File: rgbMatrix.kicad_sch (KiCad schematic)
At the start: 166 parts

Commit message: Right LED Driver almost connected
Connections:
- net CS1: now also R_B1.1; no longer R_G1.1
- net CS10: now also R_B4.1; no longer R_G4.1
- net CS12: now also R_G4.1; no longer R_B4.1
- net CS13: now also R_B5.1; no longer R_G5.1
- net CS15: now also R_G5.1; no longer R_B5.1
- net CS16: now also R_B6.1; no longer R_G6.1
- net CS18: now also R_G6.1; no longer R_B6.1
- net CS19: now also R_B7.1; no longer R_G7.1
- net CS21: now also R_G7.1; no longer R_B7.1
- net CS22: now also R_B8.1; no longer R_G8.1
- net CS24: now also R_G8.1; no longer R_B8.1
- net CS25: now also R_B9.1; no longer R_G9.1
- net CS27: now also R_G9.1; no longer R_B9.1
- net CS28: now also R_B10.1; no longer R_G10.1
- net CS3: now also R_G1.1; no longer R_B1.1
- net CS30: now also R_G10.1; no longer R_B10.1
- net CS4: now also R_B2.1; no longer R_G2.1
- net CS40: now also R_B11.1; no longer R_G17.1
- net CS41: now also R_R11.1; no longer R_R17.1
- net CS42: now also R_G11.1; no longer R_B17.1
- net CS43: now also R_B12.1; no longer R_G16.1
- net CS44: now also R_R12.1; no longer R_R16.1
- net CS45: now also R_G12.1; no longer R_B16.1
- net CS46: now also R_B13.1; no longer R_G15.1
- net CS47: now also R_R13.1; no longer R_R15.1
- net CS48: now also R_G13.1; no longer R_B15.1
- net CS49: now also R_B14.1; no longer R_G14.1
- net CS51: now also R_G14.1; no longer R_B14.1
- net CS52: now also R_B15.1; no longer R_G13.1
- net CS53: now also R_R15.1; no longer R_R13.1
- net CS54: now also R_G15.1; no longer R_B13.1
- net CS55: now also R_B16.1; no longer R_G12.1
- net CS56: now also R_R16.1; no longer R_R12.1
- net CS57: now also R_G16.1; no longer R_B12.1
- net CS58: now also R_B17.1; no longer R_G11.1
- net CS59: now also R_R17.1; no longer R_R11.1
- net CS6: now also R_G2.1; no longer R_B2.1
- net CS60: now also R_G17.1; no longer R_B11.1
- net CS7: now also R_B3.1; no longer R_G3.1
- net CS9: now also R_G3.1; no longer R_B3.1

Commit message: Routing Finished
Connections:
- net CS1: now also R_B9.1; no longer R_B1.1
- net CS10: now also R_B2.1; no longer R_B4.1
- net CS11: now also R_R2.1; no longer R_R4.1
- net CS12: now also R_G2.1; no longer R_G4.1
- net CS13: now also R_B3.1; no longer R_B5.1
- net CS14: now also R_R3.1; no longer R_R5.1
- net CS15: now also R_G3.1; no longer R_G5.1
- net CS16: now also R_B4.1; no longer R_B6.1
- net CS17: now also R_R4.1; no longer R_R6.1
- net CS18: now also R_G4.1; no longer R_G6.1
- net CS19: now also R_B5.1; no longer R_B7.1
- net CS2: now also R_R9.1; no longer R_R1.1
- net CS20: now also R_R5.1; no longer R_R7.1
- net CS21: now also R_G5.1; no longer R_G7.1
- net CS22: now also R_B6.1; no longer R_B8.1
- net CS23: now also R_R6.1; no longer R_R8.1
- net CS24: now also R_G6.1; no longer R_G8.1
- net CS25: now also R_B7.1; no longer R_B9.1
- net CS26: now also R_R7.1; no longer R_R9.1
- net CS27: now also R_G7.1; no longer R_G9.1
- net CS28: now also R_B8.1; no longer R_B10.1
- net CS29: now also R_R8.1; no longer R_R10.1
- net CS3: now also R_G9.1; no longer R_G1.1
- net CS30: now also R_G8.1; no longer R_G10.1
- net CS4: now also R_B10.1; no longer R_B2.1
- net CS5: now also R_R10.1; no longer R_R2.1
- net CS6: now also R_G10.1; no longer R_G2.1
- net CS7: now also R_B1.1; no longer R_B3.1
- net CS8: now also R_R1.1; no longer R_R3.1
- net CS9: now also R_G1.1; no longer R_G3.1

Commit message: Rearranged LED Drivers
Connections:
- net CS1: now also R_B7.1; no longer R_B9.1
- net CS10: now also R_B10.1; no longer R_B2.1
- net CS11: now also R_R10.1; no longer R_R2.1
- net CS12: now also R_G10.1; no longer R_G2.1
- net CS13: now also R_B1.1; no longer R_B3.1
- net CS14: now also R_R1.1; no longer R_R3.1
- net CS15: now also R_G1.1; no longer R_G3.1
- net CS16: now also R_B2.1; no longer R_B4.1
- net CS17: now also R_R2.1; no longer R_R4.1
- net CS18: now also R_G2.1; no longer R_G4.1
- net CS19: now also R_B3.1; no longer R_B5.1
- net CS2: now also R_R7.1; no longer R_R9.1
- net CS20: now also R_R3.1; no longer R_R5.1
- net CS21: now also R_G3.1; no longer R_G5.1
- net CS22: now also R_B4.1; no longer R_B6.1
- net CS23: now also R_R4.1; no longer R_R6.1
- net CS24: now also R_G4.1; no longer R_G6.1
- net CS25: now also R_B5.1; no longer R_B7.1
- net CS26: now also R_R5.1; no longer R_R7.1
- net CS27: now also R_G5.1; no longer R_G7.1
- net CS28: now also R_B6.1; no longer R_B8.1
- net CS29: now also R_R6.1; no longer R_R8.1
- net CS3: now also R_G7.1; no longer R_G9.1
- net CS30: now also R_G6.1; no longer R_G8.1
- net CS31: now also R_B15.1; no longer R_B18.1
- net CS32: now also R_G15.1; no longer R_R18.1
- net CS33: now also R_R15.1; no longer R_G18.1
- net CS34: now also R_B16.1; no longer R_B19.1
- net CS35: now also R_G16.1; no longer R_R19.1
- net CS36: now also R_R16.1; no longer R_G19.1
- net CS37: now also R_B17.1; no longer R_R20.1
- net CS38: now also R_G17.1; no longer R_G20.1
- net CS39: now also R_R17.1; no longer R_B20.1
- net CS4: now also R_B8.1; no longer R_B10.1
- net CS40: now also R_B18.1; no longer R_B11.1
- net CS41: now also R_R18.1; no longer R_R11.1
- net CS42: now also R_G18.1; no longer R_G11.1
- net CS43: now also R_B19.1; no longer R_B12.1
- net CS44: now also R_R19.1; no longer R_R12.1
- net CS45: now also R_G19.1; no longer R_G12.1
- net CS46: now also R_R20.1; no longer R_B13.1
- net CS47: now also R_G20.1; no longer R_R13.1
- net CS48: now also R_B20.1; no longer R_G13.1
- net CS49: now also R_B11.1; no longer R_B14.1
- net CS5: now also R_R8.1; no longer R_R10.1
- net CS50: now also R_R11.1; no longer R_R14.1
- net CS51: now also R_G11.1; no longer R_G14.1
- net CS52: now also R_B12.1; no longer R_B15.1
- net CS53: now also R_R12.1; no longer R_R15.1
- net CS54: now also R_G12.1; no longer R_G15.1
- net CS55: now also R_B13.1; no longer R_B16.1
- net CS56: now also R_R13.1; no longer R_R16.1
- net CS57: now also R_G13.1; no longer R_G16.1
- net CS58: now also R_B14.1; no longer R_B17.1
- net CS59: now also R_R14.1; no longer R_R17.1
- net CS6: now also R_G8.1; no longer R_G10.1
- net CS60: now also R_G14.1; no longer R_G17.1
- net CS7: now also R_B9.1; no longer R_B1.1
- net CS8: now also R_R9.1; no longer R_R1.1
- net CS9: now also R_G9.1; no longer R_G1.1

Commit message: Added RGB Underglow
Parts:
- added C18, C32, C34, C35, C36, C37, C38, C39, C40, C41, C42, C43, C44, C45: 104, Capacitor_SMD:C_0805_2012Metric_Pad1.18x1.45mm_HandSolder, symbol Device:C_Small
- added LED107, LED108, LED109, LED110, LED111, LED112, LED113, LED114, LED115, LED116, LED117, LED118, LED119, LED120: IN-PI55TATPRPGPB, ul_IN-PI55TATPRPGPB:IN-PI55TATPRPGPB, symbol ul_IN-PI55TATPRPGPB:IN-PI55TATPRPGPB
- added R3, R4: 500, Resistor_SMD:R_0805_2012Metric_Pad1.20x1.40mm_HandSolder, symbol Device:R_Small
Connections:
- new net: LED109.4 (DIN), LED117.2 (DOUT)
- new net: LED117.4 (DIN), LED118.2 (DOUT)
- new net: LED113.4 (DIN), LED120.2 (DOUT)
- new net: LED119.2 (DOUT), LED120.4 (DIN)
- new net: LED107.2 (DOUT), LED110.4 (DIN)
- new net: LED107.4 (DIN), LED108.2 (DOUT)
- new net: LED112.4 (DIN), LED113.2 (DOUT)
- new net: LED115.2 (DOUT), LED116.4 (DIN)
- new net: LED114.2 (DOUT), LED115.4 (DIN)
- new net: LED116.2 (DOUT), LED119.4 (DIN)
- new net: LED108.4 (DIN), LED109.2 (DOUT)
- new net: LED118.4 (DIN), R3.2
- new net: LED111.2 (DOUT), LED114.4 (DIN)
- new net: LED112.2 (DOUT), R4.2
- new net: LED110.2 (DOUT), LED111.4 (DIN)
- new net +5V: C18.1, C32.1, C34.1, C35.1, C36.1, C37.1, C38.1, C39.1, C40.1, C41.1, C42.1, C43.1, C44.1, C45.1, LED107.1 (VDD), LED108.1 (VDD), LED109.1 (VDD), LED110.1 (VDD), LED111.1 (VDD), LED112.1 (VDD), LED113.1 (VDD), LED114.1 (VDD), LED115.1 (VDD), LED116.1 (VDD), LED117.1 (VDD), LED118.1 (VDD), LED119.1 (VDD), LED120.1 (VDD)
- new net GND: C18.2, C32.2, C34.2, C35.2, C36.2, C37.2, C38.2, C39.2, C40.2, C41.2, C42.2, C43.2, C44.2, C45.2, LED107.3 (VSS), LED108.3 (VSS), LED109.3 (VSS), LED110.3 (VSS), LED111.3 (VSS), LED112.3 (VSS), LED113.3 (VSS), LED114.3 (VSS), LED115.3 (VSS), LED116.3 (VSS), LED117.3 (VSS), LED118.3 (VSS), LED119.3 (VSS), LED120.3 (VSS)
- new net RGB_DI: R3.1
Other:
- note added: "Left Side Of Keyboard"
- note added: "Right Side of Keyboard"
- note added: "Underglow"

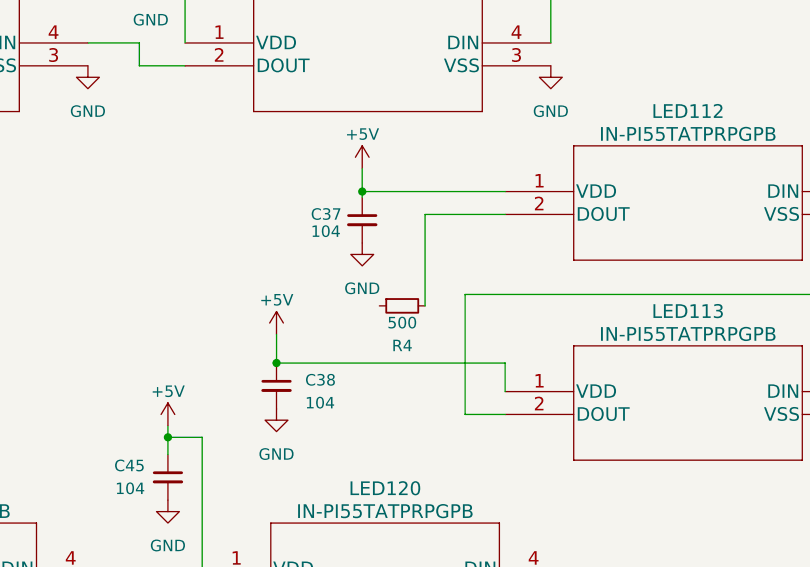
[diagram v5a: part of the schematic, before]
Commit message: Fixed Errors Relating to edge cuts
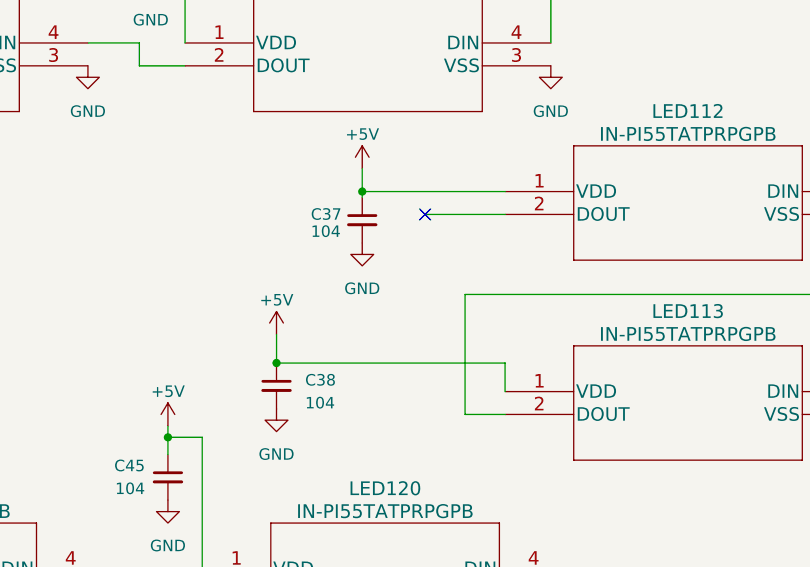
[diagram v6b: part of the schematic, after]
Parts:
- removed R4: 500, Resistor_SMD:R_0805_2012Metric_Pad1.20x1.40mm_HandSolder, symbol Device:R_Small
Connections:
- no-connect marks 0 -> 1
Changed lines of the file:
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@@
   (junction (at 147.32 276.86) (diameter 0) (color 0 0 0 0)
   )
+  (no_connect (at 337.82 353.06))
   (wire (pts (xy 190.4873 236.22) (xy 190.4873 297.1729))
     (stroke (width 0) (type default))
@@
     (stroke (width 0) (type default))
   )
-  (wire (pts (xy 337.82 353.06) (xy 337.82 363.22))
-    (stroke (width 0) (type default))
-  )
   (wire (pts (xy 147.32 52.07) (xy 166.37 52.07))
     (stroke (width 0) (type default))
@@
         )
       )
-    )
-  )
-  (symbol (lib_id "Device:R_Small") (at 335.28 363.22 90) (mirror x) (unit 1)
-    (in_bom yes) (on_board yes) (dnp no)
-    (property "Reference" "R4" (at 335.28 367.665 90)
-      (effects (font (size 1.27 1.27)))
-    )
-    (property "Value" "500" (at 335.28 365.125 90)
-      (effects (font (size 1.27 1.27)))
-    )
-    (property "Footprint" "Resistor_SMD:R_0805_2012Metric_Pad1.20x1.40mm_HandSolder" (at 335.28 363.22 0)
-      (effects (font (size 1.27 1.27)) hide)
-    )
-    (property "Datasheet" "~" (at 335.28 363.22 0)
-      (effects (font (size 1.27 1.27)) hide)
-    )
-    (pin "1")
-    (pin "2")
-    (instances
-      (project "KB-pcb-practice"
-        (path "/806fdcd7-25b2-4878-addb-1faa319c0ab0/10300069-2950-4b32-a92b-e51185ed69df"
-          (reference "R4") (unit 1)
-        )
-      )
